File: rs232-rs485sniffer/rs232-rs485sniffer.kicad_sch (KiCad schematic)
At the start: 13 parts, among them J1 supply, J2 Conn_01x05_Pin, U1 MAX232, U2 MAX485E, U3 MAX485E, U4 AMS1117-5.0

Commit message: [ADD] Add board and add management with unique rs-485 transceiver
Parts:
- removed J2: Conn_01x05_Pin, symbol Connector:Conn_01x05_Pin
- removed R1, R2: 10k, symbol Device:R
- removed U3: MAX485E, Package_SO:SOIC-8_3.9x4.9mm_P1.27mm, symbol Interface_UART:MAX485E
- added C5, C6: 100uf, Capacitor_THT:CP_Radial_D8.0mm_P3.80mm, symbol Device:C_Polarized
- added D1, D2: 1N4937, Diode_THT:D_DO-41_SOD81_P10.16mm_Horizontal, symbol Diode:1N4937
- added J2: USB_B, Connector_USB:USB_B_Lumberg_2411_02_Horizontal, symbol Connector:USB_B
- added RS485_sniffer1: Conn_01x03_Pin, TerminalBlock_Phoenix:TerminalBlock_Phoenix_MKDS-1,5-3-5.08_1x03_P5.08mm_Horizontal, symbol Connector:Conn_01x03_Pin
- C1, C2, C3, C4: footprint (none) -> Capacitor_THT:CP_Radial_D8.0mm_P3.80mm
- J1: footprint (none) -> TerminalBlock_Phoenix:TerminalBlock_Phoenix_MKDS-1,5-2_1x02_P5.00mm_Horizontal
- ReceiverRS-232: footprint (none) -> TerminalBlock_Phoenix:TerminalBlock_Phoenix_MKDS-1,5-3-5.08_1x03_P5.08mm_Horizontal
- U1: footprint (none) -> Package_DIP:DIP-16_W7.62mm_Socket_LongPads
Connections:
- net +5V: now also C6.1, J2.1 (VBUS)
- net GND: now also C5.2, C6.2, J2.4 (GND), RS485_sniffer1.1 (Pin_1)
- net at U2.4 (DI): now also D1.1 (K), D2.1 (K); no longer U1.9 (R2OUT)
- net at U2.6 (A): now also RS485_sniffer1.3 (Pin_3)
- net at U2.7 (B): now also RS485_sniffer1.2 (Pin_2)
- net at J1.1 (Pin_1), U4.3 (VI): now also C5.1
- net at U1.12 (R1OUT): now also D1.2 (A)
- new net: D2.2 (A), U1.9 (R2OUT)

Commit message: [UPD] Update schematic and add docs
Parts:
- removed D1, D2: 1N4937, Diode_THT:D_DO-41_SOD81_P10.16mm_Horizontal, symbol Diode:1N4937
- J1: value supply -> supply pin 5 GND pin 9 +12V
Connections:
- net at U2.4 (DI): now also U1.12 (R1OUT), U1.9 (R2OUT)
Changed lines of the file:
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@@
 	(wire
 		(pts
-			(xy 31.75 105.41) (xy 31.75 121.92)
-		)
-		(stroke
-			(width 0)
-			(type default)
-		)
-	)
-	(wire
-		(pts
-			(xy 31.75 86.36) (xy 31.75 97.79)
+			(xy 31.75 86.36) (xy 31.75 121.92)
 		)
 		(stroke
@@
 	(wire
 		(pts
-			(xy 62.23 100.33) (xy 62.23 91.44)
+			(xy 62.23 91.44) (xy 62.23 121.92)
 		)
 		(stroke
@@
 		(pts
 			(xy 170.18 67.31) (xy 172.72 67.31)
-		)
-		(stroke
-			(width 0)
-			(type default)
-		)
-	)
-	(wire
-		(pts
-			(xy 62.23 121.92) (xy 62.23 107.95)
 		)
 		(stroke
@@
 	)
 	(symbol
-		(lib_id "Diode:1N4937")
-		(at 31.75 101.6 90)
-		(unit 1)
-		(exclude_from_sim no)
-		(in_bom yes)
-		(on_board yes)
-		(dnp no)
-		(fields_autoplaced yes)
-		(property "Reference" "D1"
-			(at 34.29 100.3299 90)
-			(effects
-				(font
-					(size 1.27 1.27)
-				)
-				(justify right)
-			)
-		)
-		(property "Value" "1N4937"
-			(at 34.29 102.8699 90)
-			(effects
-				(font
-					(size 1.27 1.27)
-				)
-				(justify right)
-			)
-		)
-		(property "Footprint" "Diode_THT:D_DO-41_SOD81_P10.16mm_Horizontal"
-			(at 31.75 101.6 0)
-			(effects
-				(font
-					(size 1.27 1.27)
-				)
-				(hide yes)
-			)
-		)
-		(property "Datasheet" "https://www.vishay.com/docs/88508/1n4933.pdf"
-			(at 31.75 101.6 0)
-			(effects
-				(font
-					(size 1.27 1.27)
-				)
-				(hide yes)
-			)
-		)
-		(property "Description" "Fast Switching Plastic Rectifier, VRRM 600V, IF(AV) 1.0A, trr 200ns, DO-41"
-			(at 31.75 101.6 0)
-			(effects
-				(font
-					(size 1.27 1.27)
-				)
-				(hide yes)
-			)
-		)
-		(property "Sim.Device" "D"
-			(at 31.75 101.6 0)
-			(effects
-				(font
-					(size 1.27 1.27)
-				)
-				(hide yes)
-			)
-		)
-		(property "Sim.Pins" "1=K 2=A"
-			(at 31.75 101.6 0)
-			(effects
-				(font
-					(size 1.27 1.27)
-				)
-				(hide yes)
-			)
-		)
-		(pin "2"
-		)
-		(pin "1"
-		)
-		(instances
-			(project ""
-				(path "/f6392360-3747-4a58-917c-5b5441ac4e7b"
-					(reference "D1")
-					(unit 1)
-				)
-			)
-		)
-	)
-	(symbol
 		(lib_id "power:+5V")
 		(at 95.25 132.08 0)
@@
 			)
 		)
-		(property "Value" "supply"
+		(property "Value" "supply pin 5 GND pin 9 +12V"
 			(at 140.335 64.77 0)
 			(effects
@@
 					(unit 1)
 				)
-			)
-		)
-	)
-	(symbol
-		(lib_id "Diode:1N4937")
-		(at 62.23 104.14 90)
-		(unit 1)
-		(exclude_from_sim no)
-		(in_bom yes)
-		(on_board yes)
-		(dnp no)
-		(fields_autoplaced yes)
-		(property "Reference" "D2"
-			(at 64.77 102.8699 90)
-			(effects
-				(font
-					(size 1.27 1.27)
-				)
-				(justify right)
-			)
-		)
-		(property "Value" "1N4937"
-			(at 64.77 105.4099 90)
-			(effects
-				(font
-					(size 1.27 1.27)
-				)
-				(justify right)
-			)
-		)
-		(property "Footprint" "Diode_THT:D_DO-41_SOD81_P10.16mm_Horizontal"
-			(at 62.23 104.14 0)
-			(effects
-				(font
-					(size 1.27 1.27)
-				)
-				(hide yes)
-			)
-		)
-		(property "Datasheet" "https://www.vishay.com/docs/88508/1n4933.pdf"
-			(at 62.23 104.14 0)
-			(effects
-				(font
-					(size 1.27 1.27)
-				)
-				(hide yes)
-			)
-		)
-		(property "Description" "Fast Switching Plastic Rectifier, VRRM 600V, IF(AV) 1.0A, trr 200ns, DO-41"
-			(at 62.23 104.14 0)
-			(effects
-				(font
-					(size 1.27 1.27)
-				)
-				(hide yes)
-			)
-		)
-		(property "Sim.Device" "D"
-			(at 62.23 104.14 0)
-			(effects
-				(font
-					(size 1.27 1.27)
-				)
-				(hide yes)
-			)
-		)
-		(property "Sim.Pins" "1=K 2=A"
-			(at 62.23 104.14 0)
-			(effects
-				(font
-					(size 1.27 1.27)
-				)
-				(hide yes)
-			)
-		)
-		(pin "2"
-		)
-		(pin "1"
-		)
-		(instances
-			(project "rs232-rs485sniffer"
-				(path "/f6392360-3747-4a58-917c-5b5441ac4e7b"
-					(reference "D2")
-					(unit 1)
-				)

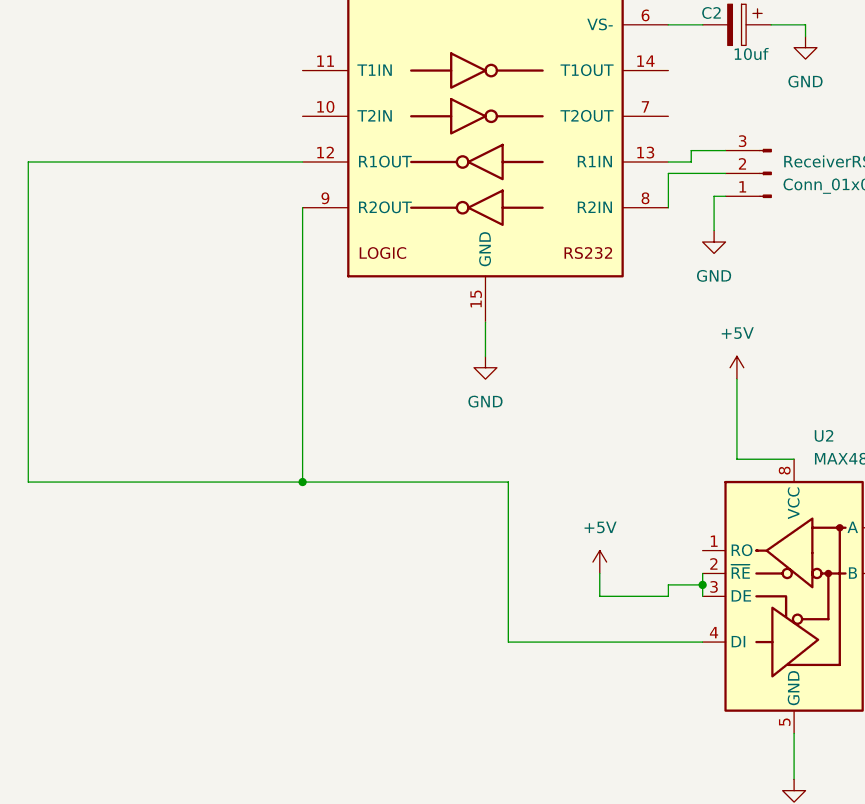
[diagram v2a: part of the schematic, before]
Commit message: [ADD] Add 2 resistor to moderate signal of TTL
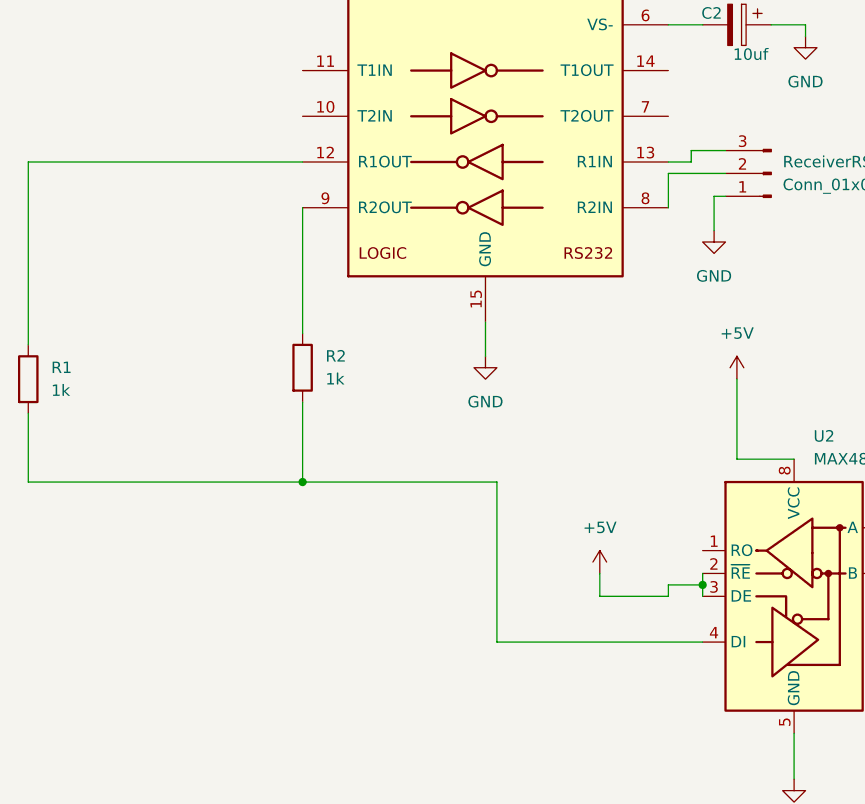
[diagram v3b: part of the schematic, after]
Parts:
- added R1, R2: 1k, Inductor_SMD:L_1206_3216Metric_Pad1.22x1.90mm_HandSolder, symbol Device:R
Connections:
- new net: R1.2, R2.2, U2.4 (DI)
- new net: R1.1, U1.12 (R1OUT)
- new net: R2.1, U1.9 (R2OUT)
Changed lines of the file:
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@@
 	(wire
 		(pts
-			(xy 31.75 86.36) (xy 31.75 121.92)
+			(xy 31.75 86.36) (xy 31.75 106.68)
 		)
 		(stroke
@@
 	(wire
 		(pts
+			(xy 31.75 114.3) (xy 31.75 121.92)
+		)
+		(stroke
+			(width 0)
+			(type default)
+		)
+	)
+	(wire
+		(pts
 			(xy 132.08 135.89) (xy 135.89 135.89)
 		)
@@
 	(wire
 		(pts
+			(xy 83.82 139.7) (xy 106.68 139.7)
+		)
+		(stroke
+			(width 0)
+			(type default)
+		)
+	)
+	(wire
+		(pts
 			(xy 123.19 62.23) (xy 115.57 62.23)
 		)
@@
 	(wire
 		(pts
-			(xy 85.09 139.7) (xy 85.09 121.92)
+			(xy 83.82 139.7) (xy 83.82 121.92)
 		)
 		(stroke
@@
 	(wire
 		(pts
-			(xy 62.23 91.44) (xy 62.23 121.92)
+			(xy 62.23 91.44) (xy 62.23 105.41)
 		)
 		(stroke
@@
 	(wire
 		(pts
-			(xy 85.09 121.92) (xy 62.23 121.92)
+			(xy 83.82 121.92) (xy 62.23 121.92)
 		)
 		(stroke
@@
 	(wire
 		(pts
-			(xy 106.68 139.7) (xy 85.09 139.7)
-		)
-		(stroke
-			(width 0)
-			(type default)
-		)
-	)
-	(wire
-		(pts
 			(xy 123.19 38.1) (xy 123.19 62.23)
 		)
@@
 		(pts
 			(xy 82.55 38.1) (xy 123.19 38.1)
+		)
+		(stroke
+			(width 0)
+			(type default)
+		)
+	)
+	(wire
+		(pts
+			(xy 62.23 113.03) (xy 62.23 121.92)
 		)
 		(stroke
@@
 					(unit 1)
 				)
+			)
+		)
+	)
+	(symbol
+		(lib_id "Device:R")
+		(at 31.75 110.49 0)
+		(unit 1)
+		(exclude_from_sim no)
+		(in_bom yes)
+		(on_board yes)
+		(dnp no)
+		(fields_autoplaced yes)
+		(property "Reference" "R1"
+			(at 34.29 109.2199 0)
+			(effects
+				(font
+					(size 1.27 1.27)
+				)
+				(justify left)
+			)
+		)
+		(property "Value" "1k"
+			(at 34.29 111.7599 0)
+			(effects
+				(font
+					(size 1.27 1.27)
+				)
+				(justify left)
+			)
+		)
+		(property "Footprint" "Inductor_SMD:L_1206_3216Metric_Pad1.22x1.90mm_HandSolder"
+			(at 29.972 110.49 90)
+			(effects
+				(font
+					(size 1.27 1.27)
+				)
+				(hide yes)
+			)
+		)
+		(property "Datasheet" "~"
+			(at 31.75 110.49 0)
+			(effects
+				(font
+					(size 1.27 1.27)
+				)
+				(hide yes)
+			)
+		)
+		(property "Description" "Resistor"
+			(at 31.75 110.49 0)
+			(effects
+				(font
+					(size 1.27 1.27)
+				)
+				(hide yes)
+			)
+		)
+		(pin "1"
+		)
+		(pin "2"
+		)
+		(instances
+			(project ""
+				(path "/f6392360-3747-4a58-917c-5b5441ac4e7b"
+					(reference "R1")
+					(unit 1)
+				)
+			)
+		)
+	)
+	(symbol
+		(lib_id "Device:R")
+		(at 62.23 109.22 0)
+		(unit 1)
+		(exclude_from_sim no)
+		(in_bom yes)
+		(on_board yes)
+		(dnp no)
+		(fields_autoplaced yes)
+		(property "Reference" "R2"
+			(at 64.77 107.9499 0)
+			(effects
+				(font
+					(size 1.27 1.27)
+				)
+				(justify left)
+			)
+		)
+		(property "Value" "1k"
+			(at 64.77 110.4899 0)
+			(effects
+				(font
+					(size 1.27 1.27)
+				)
+				(justify left)
+			)
+		)
+		(property "Footprint" "Inductor_SMD:L_1206_3216Metric_Pad1.22x1.90mm_HandSolder"
+			(at 60.452 109.22 90)
+			(effects
+				(font
+					(size 1.27 1.27)
+				)
+				(hide yes)
+			)
+		)
+		(property "Datasheet" "~"
+			(at 62.23 109.22 0)
+			(effects
+				(font
+					(size 1.27 1.27)
+				)
+				(hide yes)
+			)
+		)
+		(property "Description" "Resistor"
+			(at 62.23 109.22 0)
+			(effects
+				(font
+					(size 1.27 1.27)
+				)
+				(hide yes)
+			)
+		)
+		(pin "1"
+		)
+		(pin "2"
+		)
+		(instances
+			(project ""
+				(path "/f6392360-3747-4a58-917c-5b5441ac4e7b"
+					(reference "R2")
+					(unit 1)
+				)
